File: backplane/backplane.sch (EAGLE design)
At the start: 16 parts, among them J1 5535070-4, J2 5535070-4, J3 5535070-4, J4 5535070-4, J5 5535070-4, J6 5535070-4, J7 5535070-4, J8 5535070-4, U1 LM1084IS-5.0, U2 LM1084IS-3.3

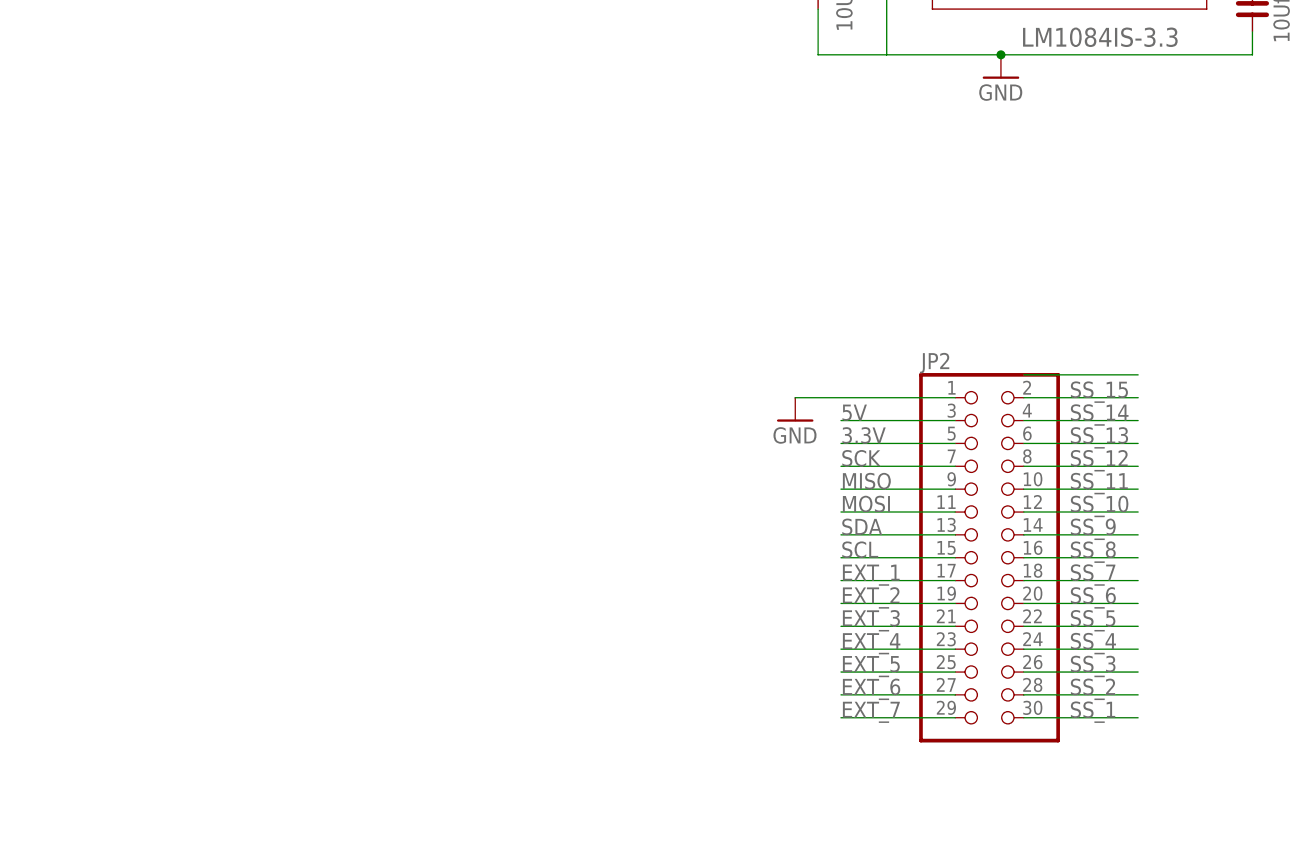
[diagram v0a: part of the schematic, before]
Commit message: worked on the perfboard prototype card, validated the valves board mechanism
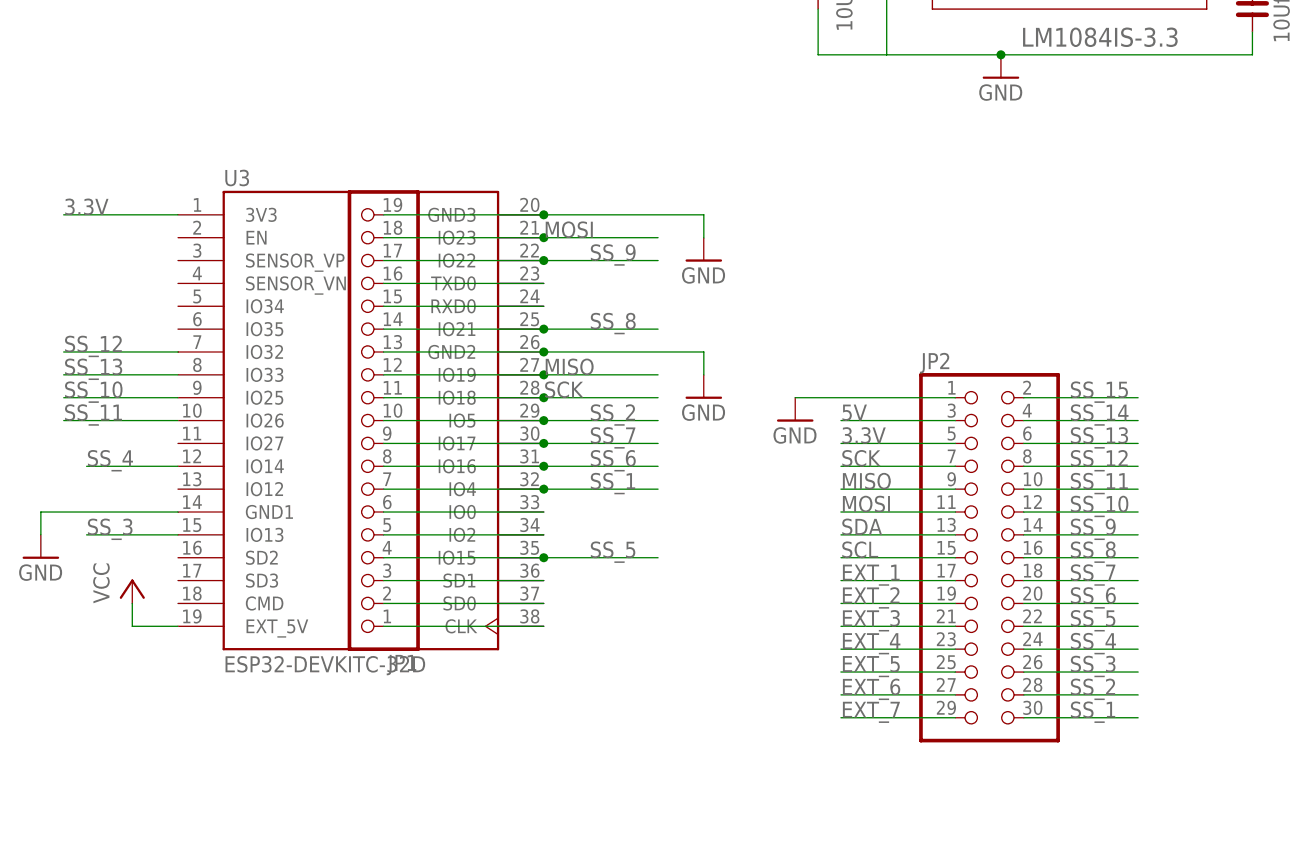
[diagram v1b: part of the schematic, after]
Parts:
- added JP1: (no value), pinhead:PINHD-1X19
- added U3: ESP32-DEVKITC-32D, ESP32-DEVKITC-32D:ESP32-DEVKITC-32D
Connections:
- new net N$3: JP1.16, U3.TXD0
- new net N$4: JP1.15, U3.RXD0
- new net N$5: JP1.6, U3.IO0
- new net N$6: JP1.5, U3.IO2
- new net N$7: JP1.3, U3.SD1
- new net N$8: JP1.2, U3.SD0
- new net N$9: JP1.1, U3.CLK
- new net VCC: U3.EXT_5V
- net 3.3V: now also U3.3V3
- net GND: now also JP1.13, JP1.19, U3.GND1, U3.GND2, U3.GND3
- net MISO: now also JP1.12, U3.IO19
- net MOSI: now also JP1.18, U3.IO23
- net SCK: now also JP1.11, U3.IO18
- net SS_1: now also JP1.7, U3.IO4
- net SS_10: now also U3.IO25
- net SS_11: now also U3.IO26
- net SS_12: now also U3.IO32
- net SS_13: now also U3.IO33
- net SS_2: now also JP1.10, U3.IO5
- net SS_3: now also U3.IO13
- net SS_4: now also U3.IO14
- net SS_5: now also JP1.4, U3.IO15
- net SS_6: now also JP1.8, U3.IO16
- net SS_7: now also JP1.9, U3.IO17
- net SS_8: now also JP1.14, U3.IO21
- net SS_9: now also JP1.17, U3.IO22

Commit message: added cam data
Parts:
- C1, C3: CAPACITOR_TYPE (none) -> tantalum
- C2, C4: CAPACITOR_TYPE (none) -> mlcc
- J1, J2, J3, J4, J5, J6, J7, J8: value 5535070-4 -> 09232486825; device 5535070-4:5535070-4 -> din41612_48_pin_backplane:09232486825
- JP1: COMPONENT (none) -> female header 1x19
- U1: device LM1084IS-5.0:LM1084IS-5.0 -> LM1084IS:LM1084IS-5.0
- U2: device LM1084IS-5.0:LM1084IS-5.0 -> LM1084IS:LM1084IS-3.3
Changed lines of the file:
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@@
 </classes>
 <parts>
-<part name="J1" library="5535070-4" deviceset="5535070-4" device=""/>
-<part name="J2" library="5535070-4" deviceset="5535070-4" device=""/>
-<part name="J3" library="5535070-4" deviceset="5535070-4" device=""/>
-<part name="J4" library="5535070-4" deviceset="5535070-4" device=""/>
-<part name="J5" library="5535070-4" deviceset="5535070-4" device=""/>
-<part name="J6" library="5535070-4" deviceset="5535070-4" device=""/>
-<part name="J7" library="5535070-4" deviceset="5535070-4" device=""/>
-<part name="J8" library="5535070-4" deviceset="5535070-4" device=""/>
+<part name="J1" library="din41612_48_pin_backplane" deviceset="09232486825" device=""/>
+<part name="J2" library="din41612_48_pin_backplane" deviceset="09232486825" device=""/>
+<part name="J3" library="din41612_48_pin_backplane" deviceset="09232486825" device=""/>
+<part name="J4" library="din41612_48_pin_backplane" deviceset="09232486825" device=""/>
+<part name="J5" library="din41612_48_pin_backplane" deviceset="09232486825" device=""/>
+<part name="J6" library="din41612_48_pin_backplane" deviceset="09232486825" device=""/>
+<part name="J7" library="din41612_48_pin_backplane" deviceset="09232486825" device=""/>
+<part name="J8" library="din41612_48_pin_backplane" deviceset="09232486825" device=""/>
 <part name="GND1" library="supply1" library_urn="urn:adsk.eagle:library:371" deviceset="GND" device=""/>
 <part name="GND2" library="supply1" library_urn="urn:adsk.eagle:library:371" deviceset="GND" device=""/>
 <part name="GND3" library="supply1" library_urn="urn:adsk.eagle:library:371" deviceset="GND" device=""/>
-<part name="XS1" library="con-dg55" deviceset="2P" device=""/>
-<part name="U1" library="LM1084IS-5.0" deviceset="LM1084IS-5.0" device=""/>
-<part name="C1" library="rc-master-smd" deviceset="CP_" device="3216" value="10Uf"/>
-<part name="C2" library="rc-master-smd" deviceset="C_" device="1206" value="10Uf"/>
+<part name="XS1" library="con-dg55" deviceset="2P" device="">
+<attribute name="PURCHASE_URL_DIGIKEY" value=""/>
+</part>
+<part name="U1" library="LM1084IS" deviceset="LM1084IS-5.0" device=""/>
+<part name="C1" library="rc-master-smd" deviceset="CP_" device="3216" value="10Uf">
+<attribute name="CAPACITOR_TYPE" value="tantalum"/>
+</part>
+<part name="C2" library="rc-master-smd" deviceset="C_" device="1206" value="10Uf">
+<attribute name="CAPACITOR_TYPE" value="mlcc"/>
+</part>
 <part name="GND4" library="supply1" library_urn="urn:adsk.eagle:library:371" deviceset="GND" device=""/>
-<part name="U2" library="LM1084IS-5.0" deviceset="LM1084IS-5.0" device="" value="LM1084IS-3.3"/>
-<part name="C3" library="rc-master-smd" deviceset="CP_" device="3216" value="10Uf"/>
-<part name="C4" library="rc-master-smd" deviceset="C_" device="1206" value="10Uf"/>
+<part name="U2" library="LM1084IS" deviceset="LM1084IS-3.3" device="" value="LM1084IS-3.3"/>
+<part name="C3" library="rc-master-smd" deviceset="CP_" device="3216" value="10Uf">
+<attribute name="CAPACITOR_TYPE" value="tantalum"/>
+</part>
+<part name="C4" library="rc-master-smd" deviceset="C_" device="1206" value="10Uf">
+<attribute name="CAPACITOR_TYPE" value="mlcc"/>
+</part>
 <part name="GND5" library="supply1" library_urn="urn:adsk.eagle:library:371" deviceset="GND" device=""/>
 <part name="GND6" library="supply1" library_urn="urn:adsk.eagle:library:371" deviceset="GND" device=""/>
@@
 <part name="GND10" library="supply1" library_urn="urn:adsk.eagle:library:371" deviceset="GND" device=""/>
 <part name="GND16" library="supply1" library_urn="urn:adsk.eagle:library:371" deviceset="GND" device=""/>
-<part name="JP1" library="pinhead" library_urn="urn:adsk.eagle:library:325" deviceset="PINHD-1X19" device="" package3d_urn="urn:adsk.eagle:package:22492/2"/>
+<part name="JP1" library="pinhead" library_urn="urn:adsk.eagle:library:325" deviceset="PINHD-1X19" device="" package3d_urn="urn:adsk.eagle:package:22492/2">
+<attribute name="COMPONENT" value="female header 1x19"/>
+</part>
 </parts>
 <sheets>
@@
 <attribute name="NAME" x="5.08" y="153.67" size="1.778" layer="95"/>
 <attribute name="VALUE" x="5.08" y="143.51" size="1.778" layer="96" rot="R180" align="bottom-right"/>
+<attribute name="PURCHASE_URL_DIGIKEY" x="7.62" y="147.32" size="1.778" layer="96" display="off"/>
 </instance>
 <instance part="U1" gate="A" x="-53.34" y="152.4" smashed="yes">
@@
 <attribute name="NAME" x="-83.185" y="145.923" size="1.778" layer="95" rot="R90"/>
 <attribute name="VALUE" x="-77.47" y="139.7" size="1.778" layer="96" rot="R90"/>
+<attribute name="CAPACITOR_TYPE" x="-81.28" y="144.78" size="1.778" layer="96" rot="R90" display="off"/>
 </instance>
 <instance part="C2" gate="G$1" x="-33.02" y="142.24" smashed="yes" rot="R90">
 <attribute name="NAME" x="-34.29" y="144.145" size="1.778" layer="95" rot="R90"/>
 <attribute name="VALUE" x="-28.8925" y="138.43" size="1.778" layer="96" rot="R90"/>
+<attribute name="CAPACITOR_TYPE" x="-33.02" y="142.24" size="1.778" layer="96" rot="R90" display="off"/>
 </instance>
 <instance part="GND4" gate="1" x="-60.96" y="134.62" smashed="yes">
@@
 <attribute name="NAME" x="-85.725" y="115.443" size="1.778" layer="95" rot="R90"/>
 <attribute name="VALUE" x="-80.01" y="109.22" size="1.778" layer="96" rot="R90"/>
+<attribute name="CAPACITOR_TYPE" x="-83.82" y="114.3" size="1.778" layer="96" rot="R90" display="off"/>
 </instance>
 <instance part="C4" gate="G$1" x="-35.56" y="111.76" smashed="yes" rot="R90">
 <attribute name="NAME" x="-36.83" y="113.665" size="1.778" layer="95" rot="R90"/>
 <attribute name="VALUE" x="-31.4325" y="107.95" size="1.778" layer="96" rot="R90"/>
+<attribute name="CAPACITOR_TYPE" x="-35.56" y="111.76" size="1.778" layer="96" rot="R90" display="off"/>
 </instance>
 <instance part="GND5" gate="1" x="-63.5" y="104.14" smashed="yes">
@@
 <attribute name="NAME" x="-128.27" y="40.005" size="1.778" layer="95" rot="R180"/>
 <attribute name="VALUE" x="-128.27" y="93.98" size="1.778" layer="96" rot="R180"/>
+<attribute name="COMPONENT" x="-134.62" y="63.5" size="1.778" layer="96" rot="R180" display="off"/>
 </instance>
 </instances>
